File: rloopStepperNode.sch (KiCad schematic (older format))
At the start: 0 parts

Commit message: Remove Gimbal Functions
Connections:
- net labels added: CHA_BRAKE1_DIR, CHA_BRAKE1_STEP, CHA_BRAKE2_DIR, CHA_BRAKE2_STEP, CHB_BRAKE1_DIR, CHB_BRAKE1_STEP, CHB_BRAKE2_DIR, CHB_BRAKE2_STEP
- net labels removed: CHA_STEP1_DIR, CHA_STEP1_STEP, CHA_STEP2_DIR, CHA_STEP2_STEP, CHA_STEP3_DIR, CHA_STEP3_STEP, CHA_STEP4_DIR, CHA_STEP4_STEP, CHA_STEP5_DIR, CHA_STEP5_STEP, CHA_STEP6_DIR, CHA_STEP6_STEP, CHB_STEP1_DIR, CHB_STEP1_STEP, CHB_STEP2_DIR, CHB_STEP2_STEP, CHB_STEP3_DIR, CHB_STEP3_STEP, CHB_STEP4_DIR, CHB_STEP4_STEP, CHB_STEP5_DIR, CHB_STEP5_STEP, CHB_STEP6_DIR, CHB_STEP6_STEP, GIMBAL1_MLP, GIMBAL1_SW_EXT, GIMBAL1_SW_RET, GIMBAL1_TEMP, GIMBAL2_MLP, GIMBAL2_SW_EXT, GIMBAL2_SW_RET, GIMBAL2_TEMP, GIMBAL3_MLP, GIMBAL3_SW_EXT, GIMBAL3_SW_RET, GIMBAL3_TEMP, GIMBAL4_MLP, GIMBAL4_SW_EXT, GIMBAL4_SW_RET, GIMBAL4_TEMP
- wire segments 232 -> 168

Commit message: Update Max4948.
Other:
- note added: "MAJOR CHALLENGES:\n1. Power Muxes from a redundant source\n2. Prevent parasitic powering of a failed nodes DC bus"
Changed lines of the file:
@@
 CHB_SPI_SCK
 $Sheet
-S 5100 9750 900  300
+S 6350 2250 900  300
 U 57538173
 F0 "Sheet_Brake_420ma" 60
 F1 "StepperNode_Brake420ma.sch" 60
-F2 "BRAKE1_MLP" O R 6000 9850 60
-F3 "BRAKE2_MLP" O R 6000 9950 60
+F2 "BRAKE1_MLP" O R 7250 2350 60
+F3 "BRAKE2_MLP" O R 7250 2450 60
 $EndSheet
 Wire Wire Line
-	6000 9850 7000 9850
-Text Label 6150 9850 0    60   ~ 0
+	7250 2350 8250 2350
+Text Label 7400 2350 0    60   ~ 0
 BRAKE1_MLP
 Wire Wire Line
-	6000 9950 7000 9950
-Text Label 6150 9950 0    60   ~ 0
+	7250 2450 8250 2450
+Text Label 7400 2450 0    60   ~ 0
 BRAKE2_MLP
 Wire Wire Line
@@
 F27 "CHB_ACCEL2_NINT" I R 2100 10100 60
 $EndSheet
+Text Notes 3700 10650 0    118  ~ 0
+MAJOR CHALLENGES:\n1. Power Muxes from a redundant source\n2. Prevent parasitic powering of a failed nodes DC bus
 $EndSCHEMATC

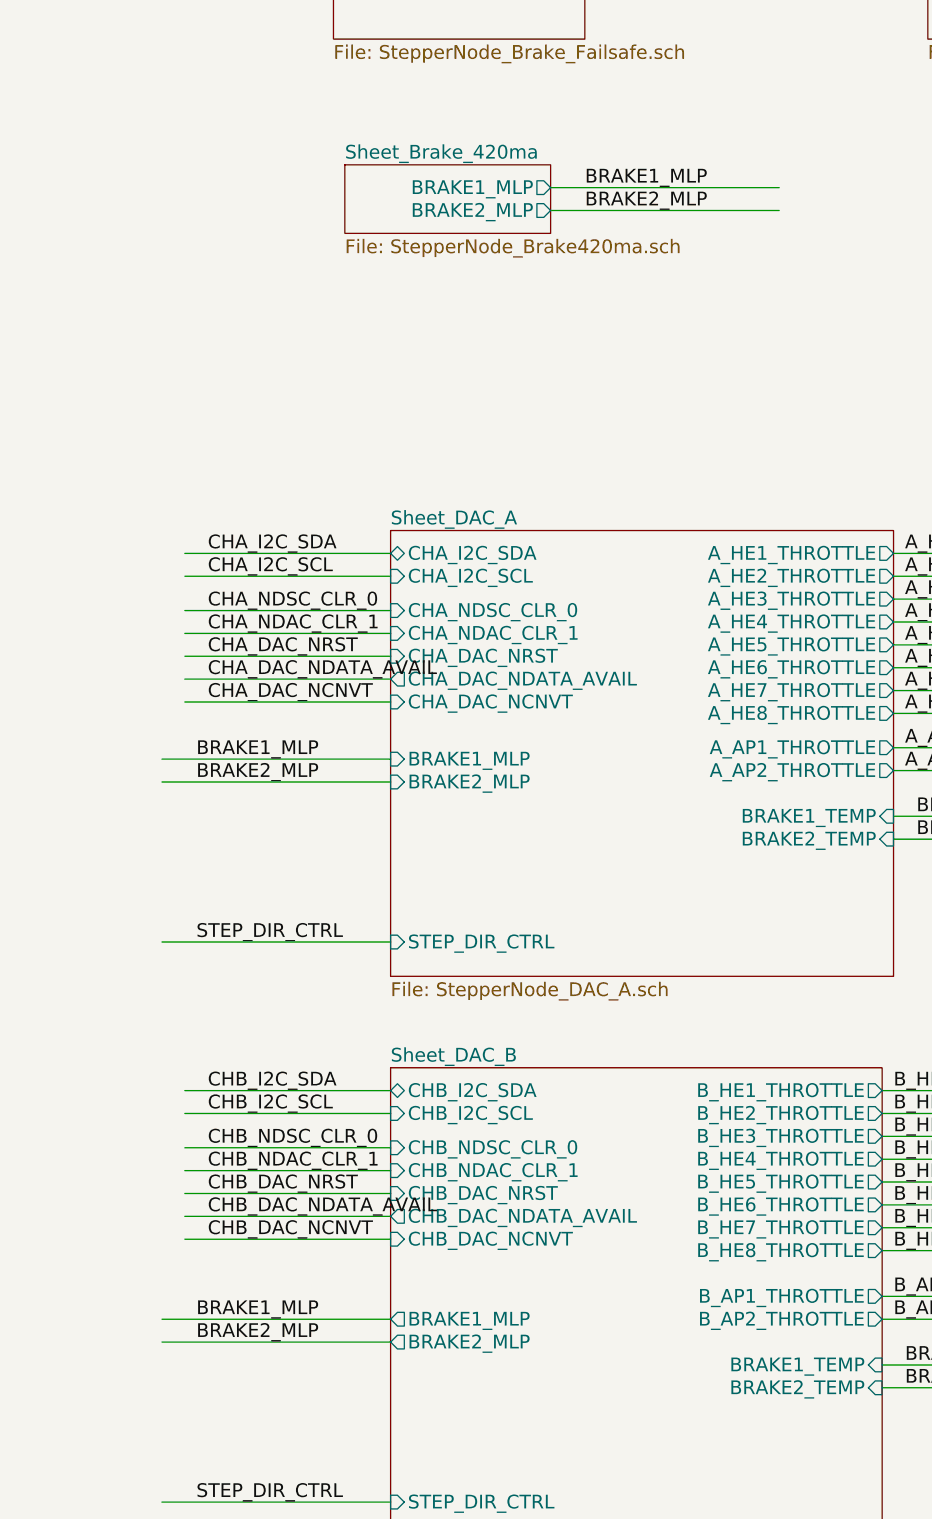
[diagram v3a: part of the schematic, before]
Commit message: Update DAC's and routed gimbal position to MCU direct.
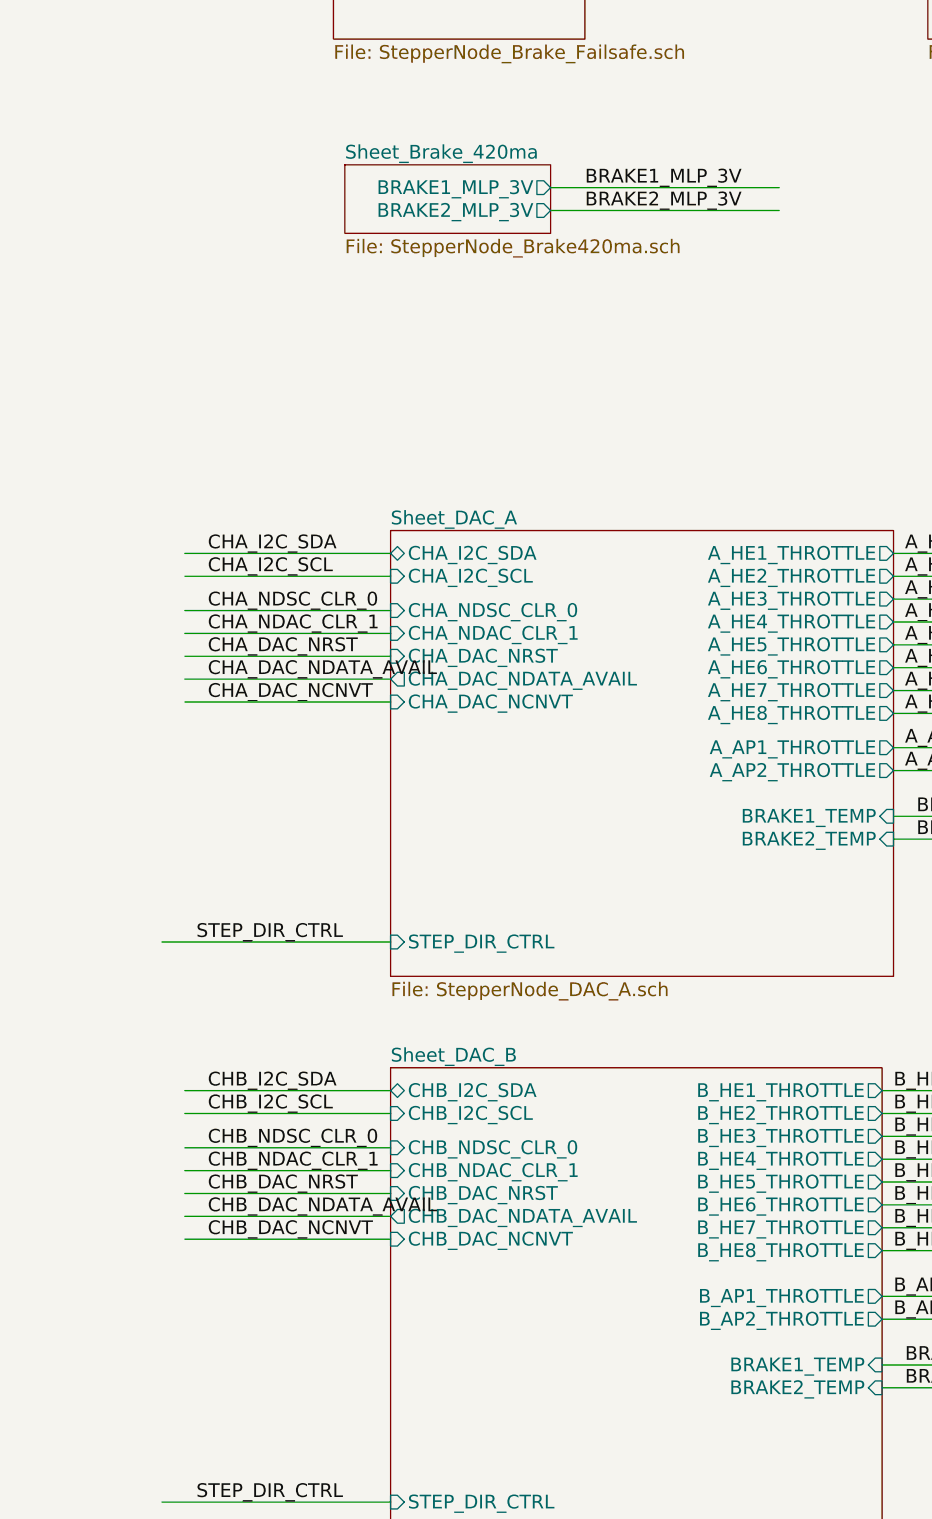
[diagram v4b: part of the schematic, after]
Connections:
- net labels added: BRAKE1_MLP_3V, BRAKE2_MLP_3V
- net labels removed: BRAKE1_MLP, BRAKE2_MLP
- wire segments 168 -> 164
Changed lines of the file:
@@
 F0 "Sheet_Brake_420ma" 60
 F1 "StepperNode_Brake420ma.sch" 60
-F2 "BRAKE1_MLP" O R 7250 2350 60
-F3 "BRAKE2_MLP" O R 7250 2450 60
+F2 "BRAKE1_MLP_3V" O R 7250 2350 60
+F3 "BRAKE2_MLP_3V" O R 7250 2450 60
 $EndSheet
 Wire Wire Line
 	7250 2350 8250 2350
 Text Label 7400 2350 0    60   ~ 0
-BRAKE1_MLP
+BRAKE1_MLP_3V
 Wire Wire Line
 	7250 2450 8250 2450
 Text Label 7400 2450 0    60   ~ 0
-BRAKE2_MLP
-Wire Wire Line
-	5550 4850 6550 4850
-Text Label 5700 4850 0    60   ~ 0
-BRAKE1_MLP
-Wire Wire Line
-	5550 4950 6550 4950
-Text Label 5700 4950 0    60   ~ 0
-BRAKE2_MLP
-Wire Wire Line
-	5550 7300 6550 7300
-Text Label 5700 7300 0    60   ~ 0
-BRAKE1_MLP
-Wire Wire Line
-	5550 7400 6550 7400
-Text Label 5700 7400 0    60   ~ 0
-BRAKE2_MLP
+BRAKE2_MLP_3V
 Wire Wire Line
 	5550 5650 6550 5650
@@
 F0 "Sheet_DAC_B" 60
 F1 "StepperNode_DAC_B.sch" 60
-F2 "BRAKE1_MLP" O L 6550 7300 60
-F3 "BRAKE2_MLP" O L 6550 7400 60
-F4 "B_HE1_THROTTLE" O R 8700 6300 60
-F5 "B_HE2_THROTTLE" O R 8700 6400 60
-F6 "B_HE3_THROTTLE" O R 8700 6500 60
-F7 "B_HE4_THROTTLE" O R 8700 6600 60
-F8 "B_HE5_THROTTLE" O R 8700 6700 60
-F9 "B_HE6_THROTTLE" O R 8700 6800 60
-F10 "B_HE7_THROTTLE" O R 8700 6900 60
-F11 "B_HE8_THROTTLE" O R 8700 7000 60
-F12 "STEP_DIR_CTRL" I L 6550 8100 60
-F13 "CHB_I2C_SDA" B L 6550 6300 60
-F14 "CHB_I2C_SCL" I L 6550 6400 60
-F15 "CHB_NDSC_CLR_0" I L 6550 6550 60
-F16 "CHB_NDAC_CLR_1" I L 6550 6650 60
-F17 "CHB_DAC_NRST" I L 6550 6750 60
-F18 "CHB_DAC_NDATA_AVAIL" O L 6550 6850 60
-F19 "CHB_DAC_NCNVT" I L 6550 6950 60
-F20 "B_AP1_THROTTLE" O R 8700 7200 60
-F21 "B_AP2_THROTTLE" O R 8700 7300 60
-F22 "BRAKE1_TEMP" I R 8700 7500 60
-F23 "BRAKE2_TEMP" I R 8700 7600 60
+F2 "B_HE1_THROTTLE" O R 8700 6300 60
+F3 "B_HE2_THROTTLE" O R 8700 6400 60
+F4 "B_HE3_THROTTLE" O R 8700 6500 60
+F5 "B_HE4_THROTTLE" O R 8700 6600 60
+F6 "B_HE5_THROTTLE" O R 8700 6700 60
+F7 "B_HE6_THROTTLE" O R 8700 6800 60
+F8 "B_HE7_THROTTLE" O R 8700 6900 60
+F9 "B_HE8_THROTTLE" O R 8700 7000 60
+F10 "STEP_DIR_CTRL" I L 6550 8100 60
+F11 "CHB_I2C_SDA" B L 6550 6300 60
+F12 "CHB_I2C_SCL" I L 6550 6400 60
+F13 "CHB_NDSC_CLR_0" I L 6550 6550 60
+F14 "CHB_NDAC_CLR_1" I L 6550 6650 60
+F15 "CHB_DAC_NRST" I L 6550 6750 60
+F16 "CHB_DAC_NDATA_AVAIL" O L 6550 6850 60
+F17 "CHB_DAC_NCNVT" I L 6550 6950 60
+F18 "B_AP1_THROTTLE" O R 8700 7200 60
+F19 "B_AP2_THROTTLE" O R 8700 7300 60
+F20 "BRAKE1_TEMP" I R 8700 7500 60
+F21 "BRAKE2_TEMP" I R 8700 7600 60
 $EndSheet
 $Sheet
@@
 F15 "A_HE7_THROTTLE" O R 8750 4550 60
 F16 "A_HE8_THROTTLE" O R 8750 4650 60
-F17 "BRAKE1_MLP" I L 6550 4850 60
-F18 "BRAKE2_MLP" I L 6550 4950 60
-F19 "STEP_DIR_CTRL" I L 6550 5650 60
-F20 "A_AP1_THROTTLE" O R 8750 4800 60
-F21 "A_AP2_THROTTLE" O R 8750 4900 60
-F22 "BRAKE1_TEMP" I R 8750 5100 60
-F23 "BRAKE2_TEMP" I R 8750 5200 60
+F17 "STEP_DIR_CTRL" I L 6550 5650 60
+F18 "A_AP1_THROTTLE" O R 8750 4800 60
+F19 "A_AP2_THROTTLE" O R 8750 4900 60
+F20 "BRAKE1_TEMP" I R 8750 5100 60
+F21 "BRAKE2_TEMP" I R 8750 5200 60
 $EndSheet
 $Sheet

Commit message: First Revision -
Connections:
- net labels added: IB_FL_RX_3V, IB_FL_TX, IB_FR_RX_3V, IB_FR_TX, IB_RL_RX_3V, IB_RL_TX
- net labels removed: CHA_IB_FL_NCS, CHA_IB_FL_NIRQ, CHA_IB_FR_NCS, CHA_IB_FR_NIRQ, CHA_IB_RL_NCS, CHA_IB_RL_NIRQ, CHA_SPI_MISO, CHA_SPI_MOSI, CHA_SPI_SCK, CHB_IB_FL_NCS, CHB_IB_FL_NIRQ, CHB_IB_FR_NCS, CHB_IB_FR_NIRQ, CHB_IB_RL_NCS, CHB_IB_RL_NIRQ, CHB_SPI_MISO, CHB_SPI_MOSI, CHB_SPI_SCK
- wire segments 164 -> 150
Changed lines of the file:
@@
 F12 "CHA_BRAKE2_STEP" O R 2100 2950 60
 F13 "CHA_WDT_PULSE" O R 2100 3100 60
-F14 "CHA_IB_FL_NIRQ" I R 2100 3400 60
-F15 "CHA_IB_RL_NIRQ" I R 2100 3500 60
-F16 "CHA_IB_FR_NIRQ" I R 2100 3600 60
-F17 "CHA_IB_RL_NCS" O R 2100 3800 60
-F18 "CHA_IB_FR_NCS" O R 2100 3900 60
-F19 "CHA_IB_FL_NCS" O R 2100 3700 60
-F20 "CHA_SPI_MOSI" O R 2100 4100 60
-F21 "CHA_SPI_MISO" I R 2100 4200 60
-F22 "CHA_SPI_SCK" O R 2100 4300 60
-F23 "CHA_AUXPROP_DIR" O R 2100 3250 60
-F24 "PUSH_INTLK_A" I R 2100 4500 60
-F25 "PUSH_INTLK_B" I R 2100 4600 60
-F26 "CHA_ACCEL1_NINT" I R 2100 4800 60
-F27 "CHA_ACCEL2_NINT" I R 2100 4900 60
+F14 "CHA_AUXPROP_DIR" O R 2100 3250 60
+F15 "PUSH_INTLK_A" I R 2100 4500 60
+F16 "PUSH_INTLK_B" I R 2100 4600 60
+F17 "CHA_ACCEL1_NINT" I R 2100 4800 60
+F18 "CHA_ACCEL2_NINT" I R 2100 4900 60
+F19 "BRAKE1_MLP_3V" I R 2100 1800 60
+F20 "BRAKE2_MLP_3V" I R 2100 1900 60
+F21 "IB_RL_TX" O R 2100 3800 60
+F22 "IB_RL_RX_3V" I R 2100 3900 60
+F23 "IB_FL_TX" O R 2100 3400 60
+F24 "IB_FL_RX_3V" I R 2100 3500 60
+F25 "IB_FR_TX" O R 2100 3600 60
+F26 "IB_FR_RX_3V" I R 2100 3700 60
 $EndSheet
 $Sheet
@@
 $EndSheet
 $Sheet
-S 10350 8650 1100 2250
+S 10350 8650 1050 800
 U 5753F632
 F0 "Sheet_IBeam_Interface" 60
 F1 "StepperNode_IBeam.sch" 60
-F2 "CHA_IB_FL_NIRQ" O L 10350 8750 60
-F3 "CHA_SPI_MOSI" I L 10350 10300 60
-F4 "CHA_SPI_MISO" O L 10350 10200 60
-F5 "CHA_SPI_SCK" I L 10350 10100 60
-F6 "CHA_IB_FL_NCS" I L 10350 9050 60
-F7 "CHA_IB_RL_NIRQ" O L 10350 8850 60
-F8 "CHA_IB_FR_NIRQ" O L 10350 8950 60
-F9 "CHA_IB_RL_NCS" I L 10350 9150 60
-F10 "CHA_IB_FR_NCS" I L 10350 9250 60
-F11 "CHB_IB_FL_NIRQ" O L 10350 9450 60
-F12 "CHB_IB_RL_NIRQ" O L 10350 9550 60
-F13 "CHB_IB_FR_NIRQ" O L 10350 9650 60
-F14 "CHB_IB_RL_NCS" I L 10350 9850 60
-F15 "CHB_IB_FR_NCS" I L 10350 9950 60
-F16 "CHB_IB_FL_NCS" I L 10350 9750 60
-F17 "CHB_SPI_MOSI" I L 10350 10700 60
-F18 "CHB_SPI_MISO" O L 10350 10600 60
-F19 "CHB_SPI_SCK" I L 10350 10500 60
+F2 "IB_FL_TX" I L 10350 8750 60
+F3 "IB_FL_RX_3V" O L 10350 8850 60
+F4 "IB_FR_TX" I L 10350 8950 60
+F5 "IB_FR_RX_3V" O L 10350 9050 60
+F6 "IB_RL_TX" I L 10350 9150 60
+F7 "IB_RL_RX_3V" O L 10350 9250 60
 $EndSheet
 $Sheet
@@
 Wire Wire Line
 	2100 3400 3000 3400
-Text Label 2200 3400 0    60   ~ 0
-CHA_IB_FL_NIRQ
 Wire Wire Line
 	2100 3500 3000 3500
-Text Label 2200 3500 0    60   ~ 0
-CHA_IB_RL_NIRQ
 Wire Wire Line
 	2100 3600 3000 3600
-Text Label 2200 3600 0    60   ~ 0
-CHA_IB_FR_NIRQ
 Wire Wire Line
 	2100 3700 3000 3700
-Text Label 2200 3700 0    60   ~ 0
-CHA_IB_FL_NCS
 Wire Wire Line
 	2100 3800 3000 3800
-Text Label 2200 3800 0    60   ~ 0
-CHA_IB_RL_NCS
 Wire Wire Line
 	2100 3900 3000 3900
-Text Label 2200 3900 0    60   ~ 0
-CHA_IB_FR_NCS
-Wire Wire Line
-	2100 4100 3000 4100
-Text Label 2200 4100 0    60   ~ 0
-CHA_SPI_MOSI
-Wire Wire Line
-	2100 4200 3000 4200
-Text Label 2200 4200 0    60   ~ 0
-CHA_SPI_MISO
-Wire Wire Line
-	2100 4300 3000 4300
-Text Label 2200 4300 0    60   ~ 0
-CHA_SPI_SCK
 Wire Wire Line
 	2100 6100 3000 6100
@@
 Text Label 2200 8200 0    60   ~ 0
 CHB_WDT_PULSE
-Wire Wire Line
-	2100 8550 3000 8550
-Text Label 2200 8550 0    60   ~ 0
-CHB_IB_FL_NIRQ
-Wire Wire Line
-	2100 8650 3000 8650
-Text Label 2200 8650 0    60   ~ 0
-CHB_IB_RL_NIRQ
-Wire Wire Line
-	2100 8750 3000 8750
-Text Label 2200 8750 0    60   ~ 0
-CHB_IB_FR_NIRQ
-Wire Wire Line
-	2100 8850 3000 8850
-Text Label 2200 8850 0    60   ~ 0
-CHB_IB_FL_NCS
-Wire Wire Line
-	2100 8950 3000 8950
-Text Label 2200 8950 0    60   ~ 0
-CHB_IB_RL_NCS
-Wire Wire Line
-	2100 9050 3000 9050
-Text Label 2200 9050 0    60   ~ 0
-CHB_IB_FR_NCS
-Wire Wire Line
-	2100 9250 3000 9250
-Text Label 2200 9250 0    60   ~ 0
-CHB_SPI_MOSI
-Wire Wire Line
-	2100 9350 3000 9350
-Text Label 2200 9350 0    60   ~ 0
-CHB_SPI_MISO
-Wire Wire Line
-	2100 9450 3000 9450
-Text Label 2200 9450 0    60   ~ 0
-CHB_SPI_SCK
 $Sheet
 S 6350 2250 900  300
@@
 B_AP2_THROTTLE
 Wire Wire Line
-	9450 9450 10350 9450
-Text Label 9550 9450 0    60   ~ 0
-CHB_IB_FL_NIRQ
-Wire Wire Line
-	9450 9550 10350 9550
-Text Label 9550 9550 0    60   ~ 0
-CHB_IB_RL_NIRQ
-Wire Wire Line
-	9450 9650 10350 9650
-Text Label 9550 9650 0    60   ~ 0
-CHB_IB_FR_NIRQ
-Wire Wire Line
-	9450 9750 10350 9750
-Text Label 9550 9750 0    60   ~ 0
-CHB_IB_FL_NCS
-Wire Wire Line
-	9450 9850 10350 9850
-Text Label 9550 9850 0    60   ~ 0
-CHB_IB_RL_NCS
-Wire Wire Line
-	9450 9950 10350 9950
-Text Label 9550 9950 0    60   ~ 0
-CHB_IB_FR_NCS
-Wire Wire Line
-	9450 10700 10350 10700
-Text Label 9550 10700 0    60   ~ 0
-CHB_SPI_MOSI
-Wire Wire Line
-	9450 10600 10350 10600
-Text Label 9550 10600 0    60   ~ 0
-CHB_SPI_MISO
-Wire Wire Line
-	9450 10500 10350 10500
-Text Label 9550 10500 0    60   ~ 0
-CHB_SPI_SCK
-Wire Wire Line
-	9450 10300 10350 10300
-Text Label 9550 10300 0    60   ~ 0
-CHA_SPI_MOSI
-Wire Wire Line
-	9450 10200 10350 10200
-Text Label 9550 10200 0    60   ~ 0
-CHA_SPI_MISO
-Wire Wire Line
-	9450 10100 10350 10100
-Text Label 9550 10100 0    60   ~ 0
-CHA_SPI_SCK
-Wire Wire Line
 	9450 8750 10350 8750
 Text Label 9550 8750 0    60   ~ 0
-CHA_IB_FL_NIRQ
+IB_FL_TX
 Wire Wire Line
 	9450 8850 10350 8850
 Text Label 9550 8850 0    60   ~ 0
-CHA_IB_RL_NIRQ
+IB_FL_RX_3V
 Wire Wire Line
 	9450 8950 10350 8950
 Text Label 9550 8950 0    60   ~ 0
-CHA_IB_FR_NIRQ
+IB_FR_TX
 Wire Wire Line
 	9450 9050 10350 9050
 Text Label 9550 9050 0    60   ~ 0
-CHA_IB_FL_NCS
+IB_FR_RX_3V
 Wire Wire Line
 	9450 9150 10350 9150
 Text Label 9550 9150 0    60   ~ 0
-CHA_IB_RL_NCS
+IB_RL_TX
 Wire Wire Line
 	9450 9250 10350 9250
 Text Label 9550 9250 0    60   ~ 0
-CHA_IB_FR_NCS
+IB_RL_RX_3V
 Wire Wire Line
 	11400 1000 10500 1000
@@
 F21 "BRAKE2_TEMP" I R 8750 5200 60
 $EndSheet
+Text Notes 3700 10650 0    118  ~ 0
+MAJOR CHALLENGES:\n1. Power Muxes from a redundant source\n2. Prevent parasitic powering of a failed nodes DC bus
+Wire Wire Line
+	2100 1800 3000 1800
+Wire Wire Line
+	2100 1900 3000 1900
+Text Label 2200 1800 0    60   ~ 0
+BRAKE1_MLP_3V
+Text Label 2200 1900 0    60   ~ 0
+BRAKE2_MLP_3V
+Text Label 2250 3400 0    60   ~ 0
+IB_FL_TX
+Text Label 2250 3500 0    60   ~ 0
+IB_FL_RX_3V
+Text Label 2250 3600 0    60   ~ 0
+IB_FR_TX
+Text Label 2250 3700 0    60   ~ 0
+IB_FR_RX_3V
+Text Label 2250 3800 0    60   ~ 0
+IB_RL_TX
+Text Label 2250 3900 0    60   ~ 0
+IB_RL_RX_3V
+Wire Wire Line
+	2100 8550 3000 8550
+Wire Wire Line
+	2100 8650 3000 8650
+Wire Wire Line
+	2100 8750 3000 8750
+Wire Wire Line
+	2100 8850 3000 8850
+Wire Wire Line
+	2100 8950 3000 8950
+Wire Wire Line
+	2100 9050 3000 9050
+Text Label 2250 8550 0    60   ~ 0
+IB_FL_TX
+Text Label 2250 8650 0    60   ~ 0
+IB_FL_RX_3V
+Text Label 2250 8750 0    60   ~ 0
+IB_FR_TX
+Text Label 2250 8850 0    60   ~ 0
+IB_FR_RX_3V
+Text Label 2250 8950 0    60   ~ 0
+IB_RL_TX
+Text Label 2250 9050 0    60   ~ 0
+IB_RL_RX_3V
 $Sheet
 S 800  6000 1300 4200
@@
 F12 "CHB_BRAKE2_STEP" O R 2100 8050 60
 F13 "CHB_WDT_PULSE" O R 2100 8200 60
-F14 "CHB_IB_FL_NIRQ" I R 2100 8550 60
-F15 "CHB_IB_RL_NIRQ" I R 2100 8650 60
-F16 "CHB_IB_FR_NIRQ" I R 2100 8750 60
-F17 "CHB_IB_RL_NCS" O R 2100 8950 60
-F18 "CHB_IB_FR_NCS" O R 2100 9050 60
-F19 "CHB_IB_FL_NCS" O R 2100 8850 60
-F20 "CHB_SPI_MOSI" O R 2100 9250 60
-F21 "CHB_SPI_MISO" I R 2100 9350 60
-F22 "CHB_SPI_SCK" O R 2100 9450 60
-F23 "CHB_AUXPROP_DIR" O R 2100 8350 60
-F24 "PUSH_INTLK_A" I R 2100 9700 60
-F25 "PUSH_INTLK_B" I R 2100 9800 60
-F26 "CHB_ACCEL1_NINT" I R 2100 10000 60
-F27 "CHB_ACCEL2_NINT" I R 2100 10100 60
-$EndSheet
-Text Notes 3700 10650 0    118  ~ 0
-MAJOR CHALLENGES:\n1. Power Muxes from a redundant source\n2. Prevent parasitic powering of a failed nodes DC bus
+F14 "CHB_AUXPROP_DIR" O R 2100 8350 60
+F15 "PUSH_INTLK_A" I R 2100 9700 60
+F16 "PUSH_INTLK_B" I R 2100 9800 60
+F17 "CHB_ACCEL1_NINT" I R 2100 10000 60
+F18 "CHB_ACCEL2_NINT" I R 2100 10100 60
+F19 "BRAKE1_MLP_3V" I R 2100 7000 60
+F20 "BRAKE2_MLP_3V" I R 2100 7100 60
+F21 "IB_FL_TX" O R 2100 8550 60
+F22 "IB_FL_RX_3V" I R 2100 8650 60
+F23 "IB_RL_TX" O R 2100 8950 60
+F24 "IB_RL_RX_3V" I R 2100 9050 60
+F25 "IB_FR_TX" O R 2100 8750 60
+F26 "IB_FR_RX_3V" I R 2100 8850 60
+$EndSheet
+Wire Wire Line
+	2100 7000 3100 7000
+Text Label 2250 7000 0    60   ~ 0
+BRAKE1_MLP_3V
+Wire Wire Line
+	2100 7100 3100 7100
+Text Label 2250 7100 0    60   ~ 0
+BRAKE2_MLP_3V
 $EndSCHEMATC

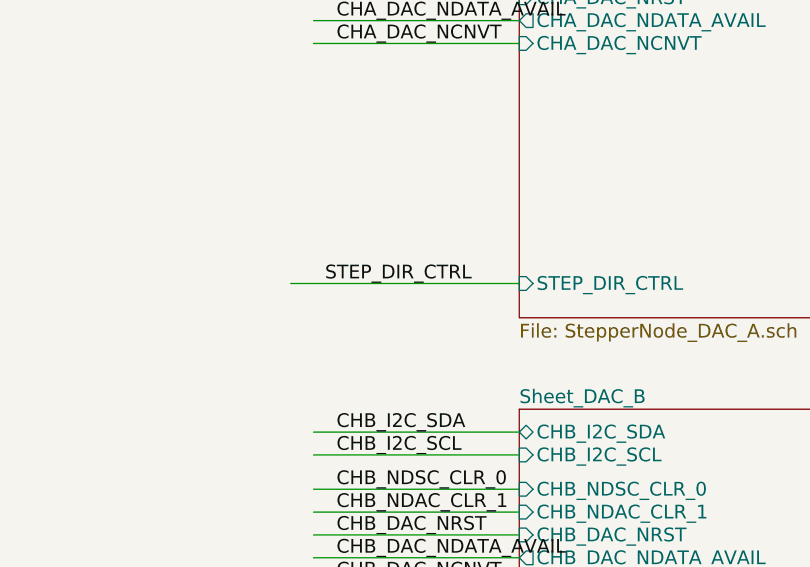
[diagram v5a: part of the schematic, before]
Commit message: Fix most ERC warnings (non-connected pins, etc)
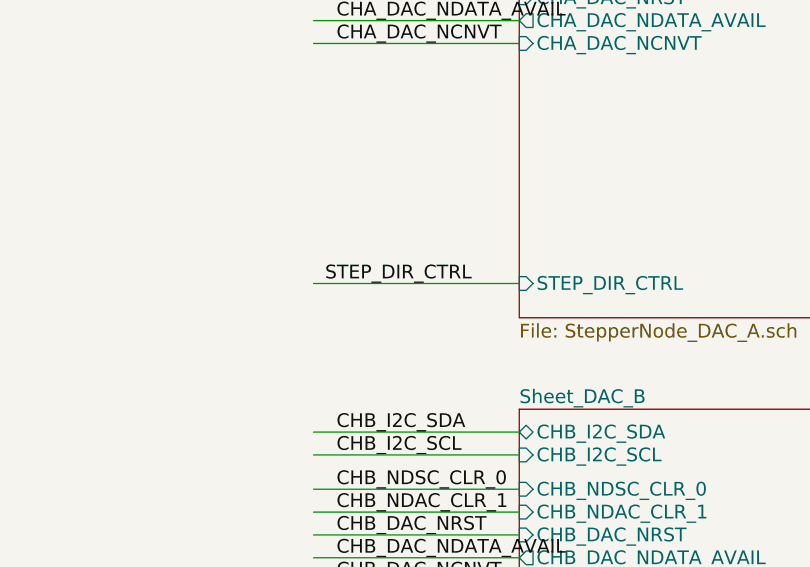
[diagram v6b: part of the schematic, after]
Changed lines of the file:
@@
 BRAKE2_MLP_3V
 Wire Wire Line
-	5550 5650 6550 5650
+	5650 5650 6550 5650
 Text Label 5700 5650 0    60   ~ 0
 STEP_DIR_CTRL
